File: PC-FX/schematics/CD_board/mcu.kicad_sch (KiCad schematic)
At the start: 35 parts, among them IC108 D78C10GF, P101 Conn_01x10, P102 Conn_01x11, P105 Conn_01x11, P107 Conn_01x11, Q105 DTC114EU3

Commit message: PCM sheet complete
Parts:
- removed C158: C, Capacitor_SMD:C_0603_1608Metric, symbol Device:C
- removed D104: D_Dual_CommonAnode_KKA, Package_TO_SOT_SMD:SOT-23, symbol Device:D_Dual_CommonAnode_KKA
- removed D105: D_Dual_CommonCathode_AAK, Package_TO_SOT_SMD:SOT-23, symbol Device:D_Dual_CommonCathode_AAK
- removed P101: Conn_01x10, Connector_JST:JST_ZE_B10B-ZESK-1D_1x10_P1.50mm_Vertical, symbol Connector_Generic:Conn_01x10
- removed P102: Conn_01x11, Connector_JST:JST_ZE_B11B-ZESK-1D_1x11_P1.50mm_Vertical, symbol Connector_Generic:Conn_01x11
- removed P105, P107: Conn_01x11, Connector_JST:JST_ZE_B02B-ZESK-1D_1x02_P1.50mm_Vertical, symbol Connector_Generic:Conn_01x02
- removed Q105: DTC114EU3, Package_TO_SOT_SMD:SOT-23, symbol PC-Engine_CDR-30:DTC114EU3
- removed R119, R121, R153, R154, R155, R156, R157, R158, R159, R513: 10k, Resistor_SMD:R_0603_1608Metric, symbol Device:R
- removed R162, R505, R506, R507, R508, R509, R510, R511, R512: 3k3, Resistor_SMD:R_0603_1608Metric, symbol Device:R
- removed R169: 47k, Resistor_SMD:R_0603_1608Metric, symbol Device:R
- removed R501: 2k2, Resistor_SMD:R_0603_1608Metric, symbol Device:R
- added C401: 100uF, Capacitor_SMD:CP_Elec_5x5.4, symbol Device:C_Polarized
- added C402, C403, C406, C409, C410, C411, C412, C413: ?, Capacitor_SMD:C_0603_1608Metric, symbol Device:C
- added CN103: Conn_01x07_Pin, symbol Connector:Conn_01x07_Pin
- added CN104: Conn_01x06_Pin, symbol Connector:Conn_01x06_Pin
- added CN105: Conn_01x03_Socket, symbol Connector:Conn_01x03_Socket
- added CN10?: Conn_01x05_Pin, symbol Connector:Conn_01x05_Pin
- added D103, D402: BAT54A, Package_TO_SOT_SMD:SOT-23, symbol Diode:BAT54A
- added IC404: 74HC125, symbol PC-FX:74HC125
- added IC405: 74LV08, symbol PC-FX:74LV08
- added IC406: 74LV04, symbol PC-FX:74LV04
- added IC407: 1951A, Package_TO_SOT_SMD:SOT-89-3, symbol PC-Engine_CDR-30:1951A
- added L401: L, symbol Device:L
- added Q106: Q_NPN_BCE, symbol Device:Q_NPN_BCE
- added Q404: 2N7002, Package_TO_SOT_SMD:SOT-23, symbol SNES:2N7002
- added R110: 3k, symbol Device:R
- added R111: 56k, symbol Device:R
- added R206, R479: 4k7, symbol Device:R
- added R407: 10k, symbol Device:R_Pack04
- added R408: 470, symbol Device:R_Pack04
- added R409: 4k7, symbol Device:R_Pack04
- added R455, R456, R457: 3k3, symbol Device:R
- added R471: 1k, symbol Device:R
- added R481: 2k2, symbol Device:R
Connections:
- net DIGIT1_EN is gone; now on net ~{SCSI_SEL}: IC108.8 (PB5)
- net PA1 is gone; now on net ~{LDON}: IC108.60 (PA1)
- net PA2 is gone; now on net FOK: IC108.61 (PA2)
- net SBSY is gone; now on net ~{SCSI_SEL}: IC108.20 (INT1)
- net +5V: no longer IC108.36 (VAREF), IC108.37 (AVDD), IC108.57 (~{STOP}), IC108.58 (VDD), IC108.64 (PA5)
- net FOK: no longer IC108.18 (PC7/CO1)
- net GND: now also C401.2, C402.1, C403.1, C406.1, C409.1, C410.1, C411.1, C412.1, C413.1, CN10?.1 (Pin_1), IC404.2, IC404.5, IC404.7 (GND), IC404.9, IC405.7 (GND), IC406.7 (GND), IC407.2 (GND), Q404.2, R407.5 (R4.2), R407.6 (R3.2), R407.7 (R2.2), R407.8 (R1.2), R455.1; no longer IC108.23 (MODE0)
- net PD0: now also IC108.49 (PD0)
- net PD1: now also IC108.50 (PD1)
- net PD2: now also IC108.51 (PD2)
- net PD3: now also IC108.52 (PD3)
- net PD4: now also IC108.53 (PD4)
- net PD5: now also IC108.54 (PD5)
- net PD6: now also IC108.55 (PD6)
- net PD7: now also IC108.56 (PD7)
- net ~{LDON}: now also IC406.3; no longer IC108.63 (PA4)
- net ~{SCSI_SEL}: no longer IC108.19 (~{NMI})
- net at IC108.14 (PC3/INT2): now also IC406.12
- net at IC108.21 (MODE1): now also R456.1
- net at IC108.28 (AN0): now also R408.8 (R1.2)
- net at IC108.29 (AN1): now also R408.7 (R2.2)
- net at IC108.30 (AN2): now also R408.6 (R3.2)
- net at IC108.31 (AN3): now also R408.5 (R4.2)
- net PF6: now reaches IC108.47 (PF6)
- net CRCF: no longer names the net of IC108.62 (PA3)
- net CRCF: now also IC404.12
- net DIGIT2_EN: no longer names the net of IC108.9 (PB6)
- net FS_RS renamed CN103_P3
- net CN103_P3: now also CN103.3 (Pin_3), R407.3 (R3.1)
- net IC108_PB2: no longer names the net of IC108.5 (PB2)
- net MCK renamed CLOCK
- net MDAT renamed DATA
- net MLT renamed XLAT
- net MODE_SELECT: no longer names the net of IC108.3 (PB0)
- net MODE_SELECT: now also R111.2
- net MUTG renamed MUTE
- net PA0: no longer names the net of IC108.59 (PA0)
- net PA0: now also IC406.1, R206.1
- net PLAY_PAUSE renamed CN103_P4
- net CN103_P4: now also CN103.4 (Pin_4), R407.4 (R4.1)
- net REPEAT renamed CN103_P2
- net CN103_P2: now also CN103.2 (Pin_2), CN104.4 (Pin_4), R407.2 (R2.1)
- net RS_EN: no longer names the net of IC108.10 (PB7)
- net STOP renamed CN103_P1
- net CN103_P1: now also CN103.1 (Pin_1), CN105.2 (Pin_2), CN105.3 (Pin_3), R407.1 (R1.1)
- net SUBQ renamed SQSO
- net XRST: no longer names the net of IC108.2 (PA7)
- net ~{GROOVE}: no longer names the net of IC108.4 (PB1)
- net ~{GROOVE}: now also R110.2
- net ~{MRST} renamed MRST
- net MRST: now also C406.2, C409.2, IC405.3, R206.2
- net ~{MUTE_EN}: no longer names the net of IC108.7 (PB4)
- net ~{MUTE_EN}: now also Q106.1 (B)
- new net: C412.2, IC405.2, Q404.3, R481.2
- new net: CN104.3 (Pin_3), D402.2
- new net: C411.2, IC405.1, IC407.3 (OUT), R479.2
- new net: IC406.10, Q404.1
- new net: CN10?.2 (Pin_2), R408.4 (R4.1), R409.5 (R4.2)
- new net: CN10?.3 (Pin_3), R408.3 (R3.1), R409.6 (R3.2)
- new net: CN10?.5 (Pin_5), R408.1 (R1.1), R409.8 (R1.2)
- new net: IC108.23 (MODE0), R457.2
- new net: IC405.8, IC406.5
- new net: IC405.10, IC406.4
- new net: CN103.7 (Pin_7), D402.3
- new net: CN10?.4 (Pin_4), R408.2 (R2.1)
- new net: IC404.11, IC405.13, R471.2
- new net: CN105.1 (Pin_1), D402.1
- new net: D103.2, R111.1
- new net: IC405.9, IC406.8
- new net: D103.1, R110.1
- new net: IC108.19 (~{NMI}), IC405.11
- new net: IC108.18 (PC7/CO1), IC405.12
- new net PCM_RST: IC406.2
- new net SBSO: IC406.9
- new net SBSO_OUT: IC406.6
- new net SLED+: CN104.1 (Pin_1)
- new net SLED-: CN104.2 (Pin_2)
- new net SPINDLE+: CN104.6 (Pin_6)
- new net SPINDLE-: CN104.5 (Pin_5)
- new net VCC: C401.1, C403.2, IC108.36 (VAREF), IC108.37 (AVDD), IC108.57 (~{STOP}), IC108.58 (VDD), IC404.1, IC404.10, IC404.14 (VCC), IC404.4, IC405.14 (VCC), IC406.14 (VCC), L401.1, R409.1 (R1.1), R409.2 (R2.1), R409.3 (R3.1), R409.4 (R4.1), R456.2, R457.1
- new net VCC2: C402.2, C410.2, C413.2, IC407.1 (VSUP), L401.2, R471.1, R479.1, R481.1
- new net ~{EXRST}: IC406.11
- no-connect marks 6 -> 5
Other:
- note added: "CN401 P13"
- note added: "CN401 P25"
- note added: "Connexions to DSP IC102"
- note added: "IC101 P19"
- note added: "IC104 P1"
- note added: "IC104 P11"
- note added: "IC104 P12"
- note added: "IC104 P2"
- note added: "IC402 P21"
- note added: "IC402 P22"
- note added: "IC402 P23"
- note added: "IC402 P24"
- note added: "IC402 P27 & IC403 P69"
- note added: "IC402 P49 & P99"
- note added: "IC402 P93"
- note added: "IC402 P95"
- note added: "IC402 P96"
- note added: "PF0-4 to IC402 PF5-6 to IC403"
- note added: "VCC2 Powers IC410, IC404, IC405, IC406, IC104?"
- note removed: "ALE latches address to PD0-7 when high and presents data when low. PD0-7 and PF0-5 are connected to SCSI chip but PF5 is also connected to the display update signal though a diode. Since writing to display requires both ~{WR} and PF5 to be low because of the logical 'OR' with diodes, it might then mean that addresses from 0000h to 1FFFh are ignored by the SCSI IC (i.e. PF5 is a chip select pin) b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"
- note removed: "DIGIT1_EN, DIGIT2_EN can't be activated to PWM the Dual seg display. DIGIT1_EN also allows to read the state of all buttons except RS as this one is active when RS_EN is on. However, it seems possible for RS_EN and DIGIT2_EN to be on at the same time. AN inputs can be configured as falling edge interrupt inputs but I doubt that's how it works as the signals are pulled down"
- note removed: "Only ~{SCSI_SEL} is connected to this cjip so other IOs must be used to inform whether we are in a command or data stage. Equally, the micro needs to know when req is asserted to read data and then ack. This might be done with PC3 as it can be configured as an interrupt. Perhaps the 8KRAM also stores the command bytes."
- note removed: "P101 Data bus is used to send 7 SEG Display data"
- note removed: "P102 connector carries mainly signals coming button signal fron the front PCB"
- note removed: "P107 is the CD lid switch. Contact is closed when lid is down Named P106 on CDR-30 Rev"
- note removed: "P107 is the connection to the sled end stop switch"
- moved on the sheet: C144, C149

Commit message: Progress mainly on SCSI chips and connections to the MCU
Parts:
- removed D103: BAT54A, Package_TO_SOT_SMD:SOT-23, symbol Diode:BAT54A
- removed Q106: Q_NPN_BCE, symbol Device:Q_NPN_BCE
- removed R110: 3k, symbol Device:R
- removed R111: 56k, symbol Device:R
- added C112, C115: ?, Capacitor_SMD:C_0603_1608Metric, symbol Device:C
- added D102: BAT54A, Package_TO_SOT_SMD:SOT-23, symbol Diode:BAT54A
- added Q106: 2N7002, Package_TO_SOT_SMD:SOT-23, symbol SNES:2N7002
- added R150: 15k, symbol Device:R
- added R151: 47k, symbol Device:R
- added R155, R177: ~, symbol Device:R
- added R196: 160k, symbol Device:R
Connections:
- net SQSO: now also IC108.9 (PB6)
- net ~{SCSI_SEL}: no longer IC108.8 (PB5)
- net at IC108.7 (PB4): now also Q106.1
- net IC402_P21: now reaches CN103.5 (Pin_5)
- net IC402_P22: now reaches CN103.6 (Pin_6)
- net IC402_P23: now reaches CN103.7 (Pin_7), D402.3
- net IC403_P69: now reaches IC404.13
- net IC401_PB0: now reaches IC108.3 (PB0)
- net IC401_PB1: now reaches IC108.4 (PB1)
- net CN401_P24: now reaches IC108.18 (PC7/CO1), IC405.12
- net IC402_P93: now reaches IC406.13
- net IC402_P95: now reaches IC108.63 (PA4)
- net IC402_P96: now reaches IC108.64 (PA5)
- net CN103_P1 renamed LID
- net ~{EEPROM_CE} renamed PF7
- new net: D102.3, R155.2
- new net: C112.1, R150.1, R151.2, R196.1
- new net: C112.2, C115.2, Q106.3, R196.2
- new net: C115.1, R151.1
- new net: R150.2, R177.1
- new net SCOR: IC108.8 (PB5)
- no-connect marks 5 -> 8
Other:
- note added: "IC402 P26 & IC403 P69"
- note added: "PF0-4 to IC402 PF5-7 to IC403"
- note removed: "IC402 P21"
- note removed: "IC402 P22"
- note removed: "IC402 P23"
- note removed: "IC402 P24"
- note removed: "IC402 P27 & IC403 P69"
- note removed: "IC402 P93"
- note removed: "IC402 P95"
- note removed: "IC402 P96"
- note removed: "PF0-4 to IC402 PF5-6 to IC403"
- moved on the sheet: C145, C146, CF101, CN103, CN104, CN105, CN10?, D402, IC108, IC405D, IC406F, R407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

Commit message: Update on DSP sheet mainly.
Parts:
- removed unit 3 of IC405
- removed unit 3 of IC406
- removed unit 2 of IC406
- removed unit 4 of IC406
- gave numbers to parts that had none: 1
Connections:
- net +5V is gone; now on net VCC: C144.2, C149.1
- net ~{SCSI_SEL} is gone; now on net SCOR: IC108.20 (INT1)
- net ~{EXRST}: now also IC404.11, IC405.13, R471.2
- net ~{INRST}: now reaches IC108.62 (PA3), IC404.12
- net IC403_P69 renamed ~{INRST_EN}
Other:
- note added: "SCSI_~{SEL} ?"
- note added: "Unpopulated conenctors"
- note removed: "CN401 P13"
- note removed: "IC101 P19"
- moved on the sheet: C112, C115, C401, C402, C403, C406, C409, C410, C411, C412, C413, CN103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

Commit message: Schematics pretty much done. Expect some mistakes but it captures enough information to help understanding its behaviour.
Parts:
- removed C112, C115, C144: ?, Capacitor_SMD:C_0603_1608Metric, symbol Device:C
- removed C149: 100uF, Capacitor_SMD:CP_Elec_5x5.4, symbol Device:C_Polarized
- removed CN104: Conn_01x06_Pin, symbol Connector:Conn_01x06_Pin
- removed D102: BAT54A, Package_TO_SOT_SMD:SOT-23, symbol Diode:BAT54A
- removed Q106: 2N7002, Package_TO_SOT_SMD:SOT-23, symbol SNES:2N7002
- removed R150: 15k, symbol Device:R
- removed R151: 47k, symbol Device:R
- removed R155, R177: ~, symbol Device:R
- removed R196: 160k, symbol Device:R
- added R459: 1k, symbol Device:R
- R455: value 3k3 -> 4k7
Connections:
- net VCC: no longer IC404.1, IC404.10, IC404.14 (VCC), IC404.4, IC405.14 (VCC), IC406.14 (VCC)
- net VCC2: now also IC404.1, IC404.10, IC404.14 (VCC), IC404.4, IC405.14 (VCC), IC406.14 (VCC), R479.2; no longer R479.1
- net ~{LDON}: now also R459.1; no longer IC108.60 (PA1)
- net ENDSW_B: now reaches D402.2
- net at C411.2, IC405.1, IC407.3 (OUT): now also R479.1; no longer R479.2
- net at IC108.29 (AN1), R408.7 (R2.2): now also R455.2
- net LID_B: now reaches CN105.1 (Pin_1), D402.1
- net IC401_PB4: now reaches IC108.7 (PB4)
- net CN103_P2 renamed ENDSW_A
- net LID renamed LID_A
- net MRST renamed ~{MRST}
- new net: IC108.60 (PA1), R459.2
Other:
- note added: "AN0, AN2 and AN3 pulled up and AN1, AN4-7 pulled-down"
- note added: "Unpopulated connectors"
- note removed: "IC104 P1"
- note removed: "IC104 P11"
- note removed: "IC104 P12"
- note removed: "IC104 P2"
- note removed: "Unpopulated conenctors"
- title: PC FX Pots Adfustment Schematics -> PC-FX CD Board Schematics
- moved on the sheet: C145, C146, C401, C402, C403, C406, C409, C410, C411, C412, C413, CF101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

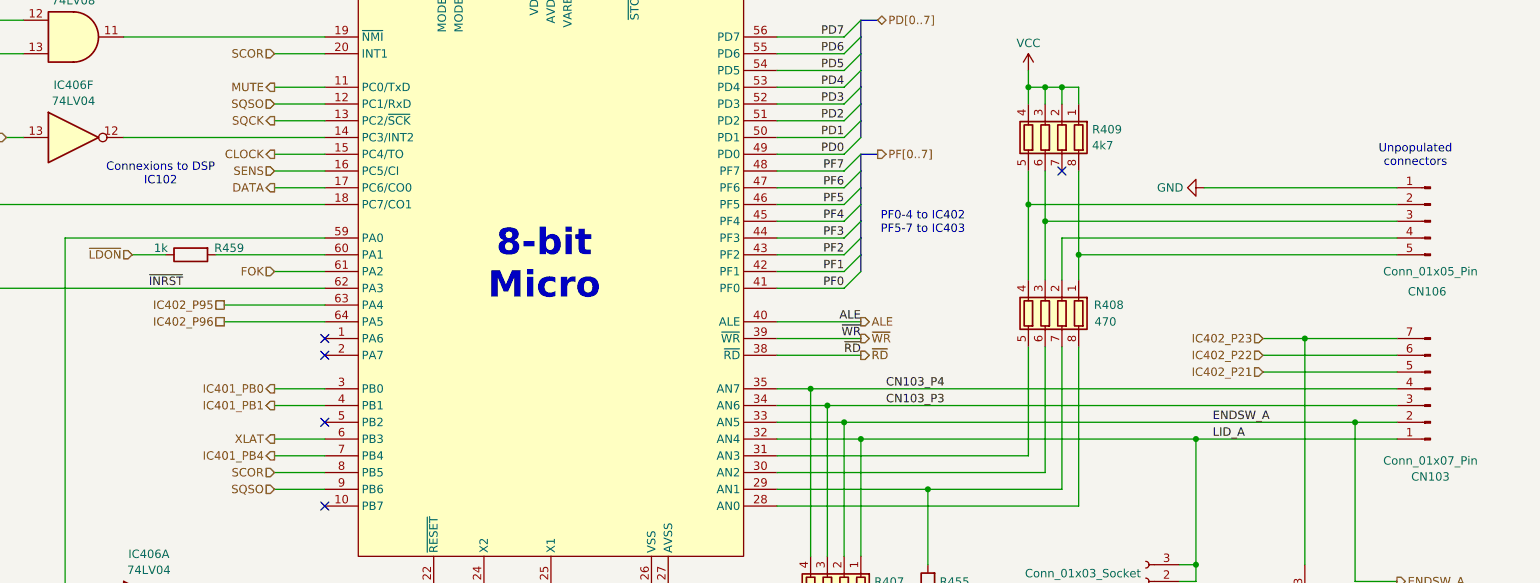
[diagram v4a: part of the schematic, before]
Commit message: Confirmed connections and fixed issues on Servo and DSP chips using similar design - Sony CDP-790
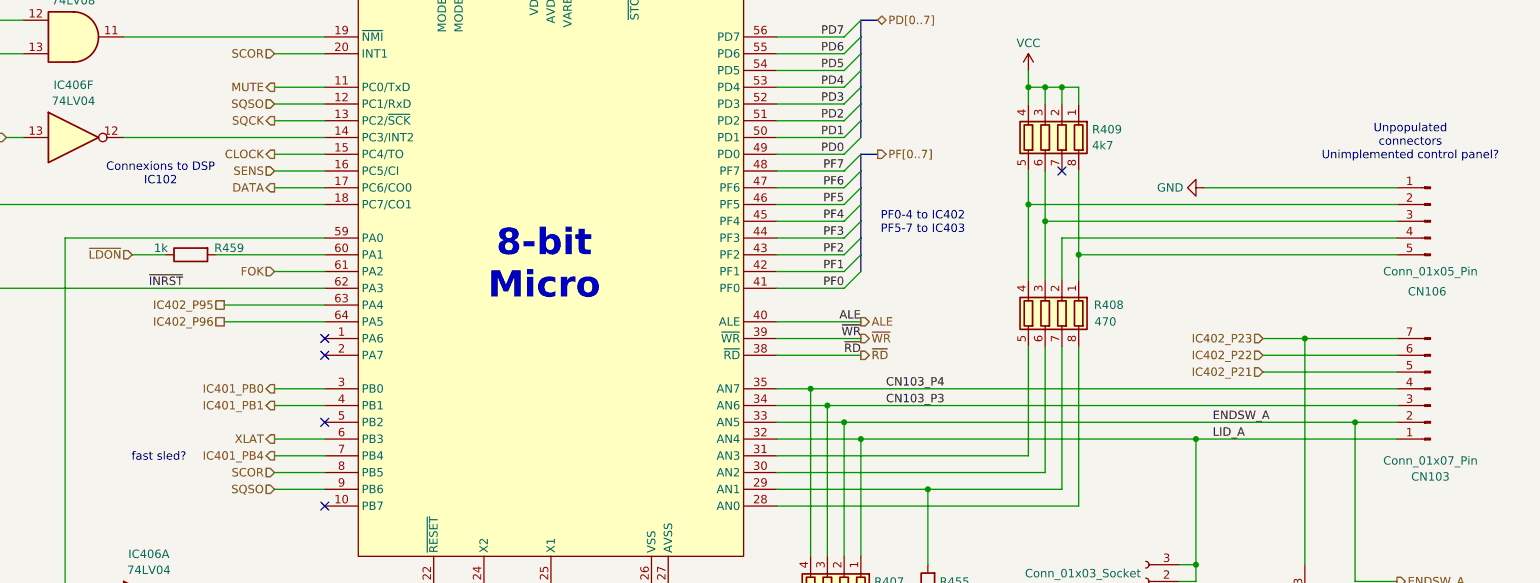
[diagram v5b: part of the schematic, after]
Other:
- note added: "Unpopulated connectors Unimplemented control panel?"
- note added: "fast sled?"
- note removed: "Unpopulated connectors"
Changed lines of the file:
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@@
+		)
+	)
+	(text "fast sled?"
+		(exclude_from_sim no)
+		(at 192.024 142.494 0)
+		(effects
+			(font
+				(size 1.27 1.27)
+			)
 		)
 	)
@@
 		)
 	)
-	(text "Unpopulated\nconnectors"
+	(text "Unpopulated\nconnectors\nUnimplemented control panel?"
 		(exclude_from_sim no)
-		(at 382.524 96.774 0)
+		(at 381.762 94.742 0)
 		(effects
 			(font

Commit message: Small update based on confirmation of SCSI control signals
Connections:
- net CN103_P3: no longer names the net of CN103.3 (Pin_3), IC108.34 (AN6), R407.3 (R3.1)
- net CN103_P4: no longer names the net of CN103.4 (Pin_4), IC108.35 (AN7), R407.4 (R4.1)
- net CN401_P24 renamed SCSI_~{SEL}
- net IC402_P23 renamed SWITCH_STROBE
- net LID_A renamed LIDSW_A
- net LID_B renamed LIDSW_B
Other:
- note added: "CN103 and CN106 are unpopulated connectors and can be used for debugging lid switch and sled end switch. Other connections are not implemented abd it would seem they could have been meant for an external control panel line on the CD-ROM2 buttons to play an audio CD."
- note added: "Logic gate power pins"
- note removed: "CN401 P25"
- note removed: "SCSI_~{SEL} ?"
- note removed: "Unpopulated connectors Unimplemented control panel?"
- moved on the sheet: C410, C411, C412, CN103, CN105, CN106, D402, IC404A, IC404B, IC404C, IC404D, IC404E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

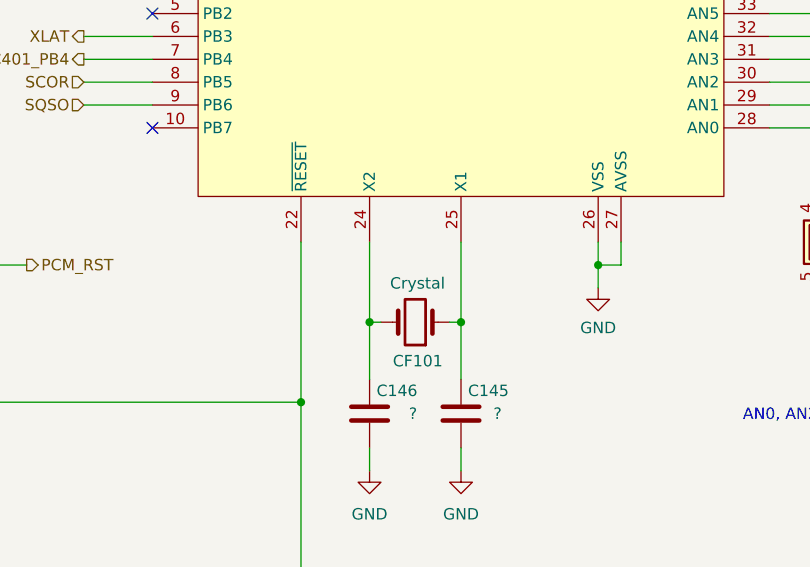
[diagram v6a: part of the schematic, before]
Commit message: Crystal frequency added + PDF of the schematics
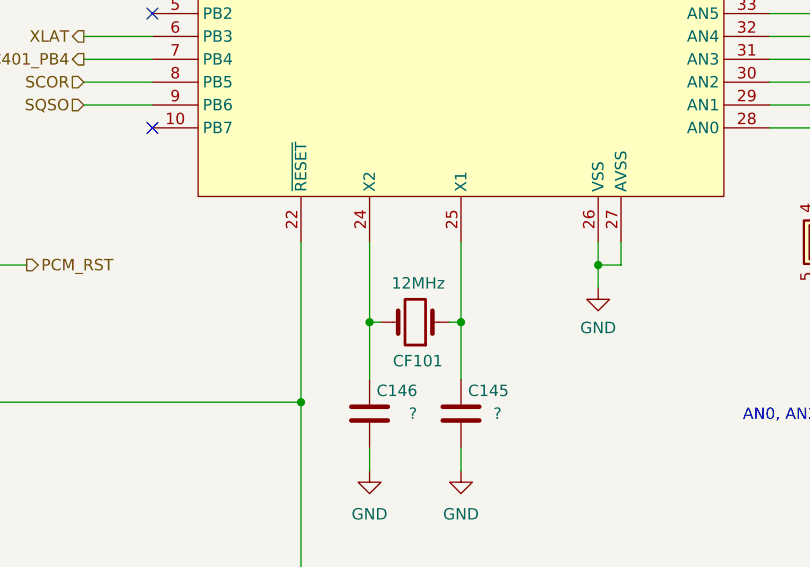
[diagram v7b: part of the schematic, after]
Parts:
- CF101: value Crystal -> 12MHz
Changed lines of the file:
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@@
 	(title_block
 		(title "PC-FX CD Board Schematics")
-		(date "2024-07-21")
+		(date "2024-07-25")
 		(rev "0.1")
 		(company "Author: Regis Galland")
@@
 			)
 		)
-		(property "Value" "Crystal"
+		(property "Value" "12MHz"
 			(at 249.682 167.132 0)
 			(effects
@@
 					(unit 1)
 				)
+			)
+			(project ""
+				(path "/28d2c364-a4dd-4270-9fde-bb67593159d8/a0eaaab6-d1f2-4662-b9ea-27212b96ad7f"
+					(reference "X401")
+					(unit 1)
+				)
